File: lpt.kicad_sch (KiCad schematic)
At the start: 25 parts, among them J6 DB25 FEMALE, K1 TE_OJS_5V_10A, Q3 BC857, U2 74HC245, U4 LM358EDR2G, U5 ACSL-6400, U7 ACSL-6400

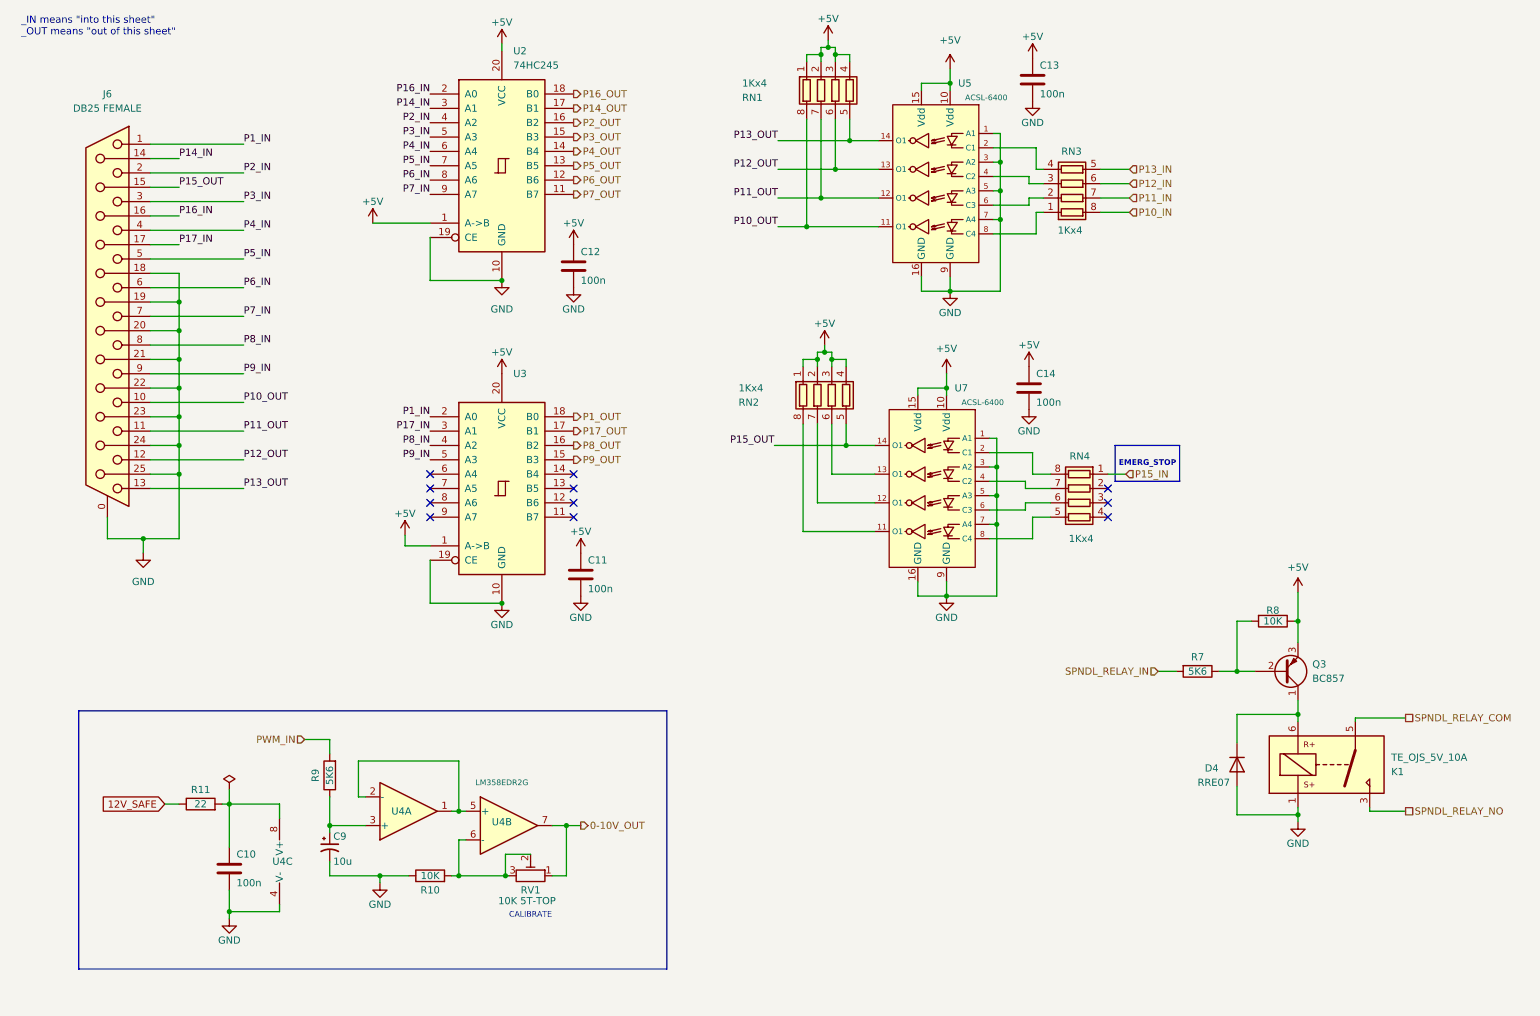
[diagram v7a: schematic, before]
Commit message: Scary file corruption turns out to be just bugs in eschema.
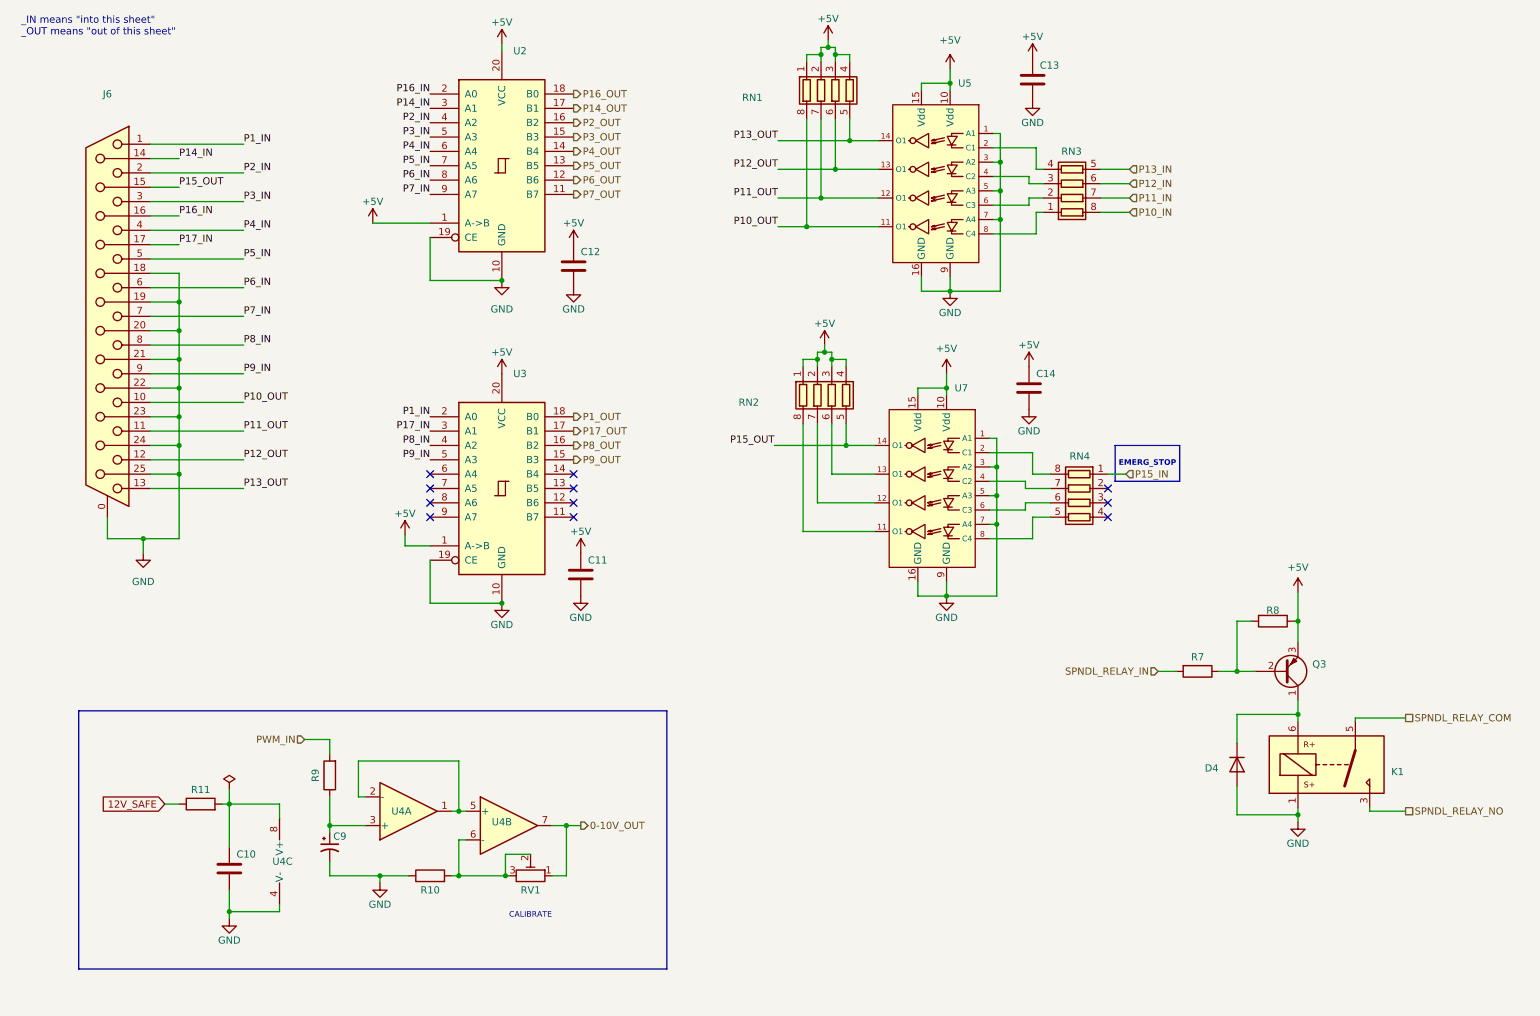
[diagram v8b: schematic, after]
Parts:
- C10, C11, C12, C13, C14: value 100n -> (none)
- C9: value 10u -> (none)
- D4: value RRE07 -> (none)
- J6: value DB25 FEMALE -> (none)
- K1: value TE_OJS_5V_10A -> (none)
- Q3: value BC857 -> (none)
- R10, R8: value 10K -> (none)
- R11: value 22 -> (none)
- R7, R9: value 5K6 -> (none)
- RN1, RN2, RN3, RN4: value 1Kx4 -> (none)
- RV1: value 10K 5T-TOP -> (none)
- U2: value 74HC245 -> (none)
- U4: value LM358EDR2G -> (none)
- U5, U7: value ACSL-6400 -> (none)
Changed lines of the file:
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@@
       (effects (font (size 1.27 1.27)) (justify left))
     )
-    (property "Value" "BC857" (id 1) (at 245.11 132.7149 0)
+    (property "Value" "" (id 1) (at 245.11 132.7149 0)
       (effects (font (size 1.27 1.27)) (justify left))
     )
@@
       (effects (font (size 1.27 1.27)) (justify left))
     )
-    (property "Value" "1Kx4" (id 1) (at 206.375 107.95 90)
+    (property "Value" "" (id 1) (at 206.375 107.95 90)
       (effects (font (size 1.27 1.27)) (justify left))
     )
@@
       (effects (font (size 1.27 1.27)) (justify left))
     )
-    (property "Value" "100n" (id 1) (at 115.57 62.23 0)
+    (property "Value" "" (id 1) (at 115.57 62.23 0)
       (effects (font (size 1.27 1.27)) (justify left))
     )
@@
       (effects (font (size 1.27 1.27)) (justify left))
     )
-    (property "Value" "100n" (id 1) (at 196.215 83.82 0)
+    (property "Value" "" (id 1) (at 196.215 83.82 0)
       (effects (font (size 1.27 1.27)) (justify left))
     )
@@
     (in_bom yes) (on_board yes)
     (property "Reference" "R10" (id 0) (at 88.9 170.18 90))
-    (property "Value" "10K" (id 1) (at 88.9 167.64 90))
+    (property "Value" "" (id 1) (at 88.9 167.64 90))
     (property "Footprint" "" (id 2) (at 88.9 169.418 90)
       (effects (font (size 1.27 1.27)) hide)
@@
     (in_bom yes) (on_board yes)
     (property "Reference" "RV1" (id 0) (at 106.68 170.18 90))
-    (property "Value" "10K 5T-TOP" (id 1) (at 106.045 172.085 90))
+    (property "Value" "" (id 1) (at 106.045 172.085 90))
     (property "Footprint" "" (id 2) (at 106.68 167.64 0)
       (effects (font (size 1.27 1.27)) hide)
@@
       (effects (font (size 1.27 1.27)) (justify left))
     )
-    (property "Value" "100n" (id 1) (at 54.61 168.91 0)
+    (property "Value" "" (id 1) (at 54.61 168.91 0)
       (effects (font (size 1.27 1.27)) (justify left))
     )
@@
     (in_bom yes) (on_board yes)
     (property "Reference" "U4" (id 0) (at 101.6 158.115 0))
-    (property "Value" "LM358EDR2G" (id 1) (at 101.6 151.13 0)
+    (property "Value" "" (id 1) (at 101.6 151.13 0)
       (effects (font (size 1 1)))
     )
@@
       (effects (font (size 1.27 1.27)) (justify left))
     )
-    (property "Value" "1Kx4" (id 1) (at 143.51 81.28 0)
+    (property "Value" "" (id 1) (at 143.51 81.28 0)
       (effects (font (size 1.27 1.27)) (justify left))
     )
@@
       (effects (font (size 1.27 1.27)) (justify left))
     )
-    (property "Value" "1Kx4" (id 1) (at 200.025 53.34 90)
+    (property "Value" "" (id 1) (at 200.025 53.34 90)
       (effects (font (size 1.27 1.27)) (justify left))
     )
@@
       (effects (font (size 1.27 1.27)) (justify left))
     )
-    (property "Value" "100n" (id 1) (at 196.85 29.21 0)
+    (property "Value" "" (id 1) (at 196.85 29.21 0)
       (effects (font (size 1.27 1.27)) (justify left))
     )
@@
     (in_bom yes) (on_board yes)
     (property "Reference" "R11" (id 0) (at 48.26 152.4 90))
-    (property "Value" "22" (id 1) (at 48.26 154.94 90))
+    (property "Value" "" (id 1) (at 48.26 154.94 90))
     (property "Footprint" "" (id 2) (at 48.26 156.718 90)
       (effects (font (size 1.27 1.27)) hide)
@@
       (effects (font (size 1.27 1.27)) (justify left))
     )
-    (property "Value" "ACSL-6400" (id 1) (at 190.5 83.82 0)
+    (property "Value" "" (id 1) (at 190.5 83.82 0)
       (effects (font (size 1 1)) (justify left))
     )
@@
     (in_bom yes) (on_board yes)
     (property "Reference" "R9" (id 0) (at 68.58 149.86 90))
-    (property "Value" "5K6" (id 1) (at 71.12 149.86 90))
+    (property "Value" "" (id 1) (at 71.12 149.86 90))
     (property "Footprint" "" (id 2) (at 72.898 149.86 90)
       (effects (font (size 1.27 1.27)) hide)
@@
       (effects (font (size 1.27 1.27)) (justify left))
     )
-    (property "Value" "1Kx4" (id 1) (at 144.145 27.305 0)
+    (property "Value" "" (id 1) (at 144.145 27.305 0)
       (effects (font (size 1.27 1.27)) (justify left))
     )
@@
       (effects (font (size 1.27 1.27)) (justify left))
     )
-    (property "Value" "74HC245" (id 1) (at 103.6194 24.13 0)
+    (property "Value" "" (id 1) (at 103.6194 24.13 0)
       (effects (font (size 1.27 1.27)) (justify left))
     )
@@
     (in_bom yes) (on_board yes)
     (property "Reference" "R8" (id 0) (at 238.125 120.65 90))
-    (property "Value" "10K" (id 1) (at 238.125 122.555 90))
+    (property "Value" "" (id 1) (at 238.125 122.555 90))
     (property "Footprint" "" (id 2) (at 238.125 120.777 90)
       (effects (font (size 1.27 1.27)) hide)
@@
     (in_bom yes) (on_board yes)
     (property "Reference" "R7" (id 0) (at 224.79 128.905 90))
-    (property "Value" "5K6" (id 1) (at 224.79 131.445 90))
+    (property "Value" "" (id 1) (at 224.79 131.445 90))
     (property "Footprint" "" (id 2) (at 224.79 129.667 90)
       (effects (font (size 1.27 1.27)) hide)
@@
       (effects (font (size 1.27 1.27)) (justify left))
     )
-    (property "Value" "ACSL-6400" (id 1) (at 191.135 29.845 0)
+    (property "Value" "" (id 1) (at 191.135 29.845 0)
       (effects (font (size 1 1)) (justify left))
     )
@@
       (effects (font (size 1.27 1.27)) (justify left))
     )
-    (property "Value" "LM358EDR2G" (id 1) (at 63.5 166.3699 0)
+    (property "Value" "" (id 1) (at 63.5 166.3699 0)
       (effects (font (size 1.27 1.27)) (justify left) hide)
     )
@@
       (effects (font (size 1.27 1.27)) (justify left))
     )
-    (property "Value" "RRE07" (id 1) (at 224.79 151.13 90)
+    (property "Value" "" (id 1) (at 224.79 151.13 90)
       (effects (font (size 1.27 1.27)) (justify left))
     )
@@
       (effects (font (size 1.27 1.27)) (justify left))
     )
-    (property "Value" "10u" (id 1) (at 71.755 165.1 0)
+    (property "Value" "" (id 1) (at 71.755 165.1 0)
       (effects (font (size 1.27 1.27)) (justify left))
     )
@@
       (effects (font (size 1.27 1.27)) (justify left))
     )
-    (property "Value" "100n" (id 1) (at 116.84 116.84 0)
+    (property "Value" "" (id 1) (at 116.84 116.84 0)
       (effects (font (size 1.27 1.27)) (justify left))
     )
@@
       (effects (font (size 1.27 1.27)) (justify left))
     )
-    (property "Value" "TE_OJS_5V_10A" (id 1) (at 259.08 146.6851 0)
+    (property "Value" "" (id 1) (at 259.08 146.6851 0)
       (effects (font (size 1.27 1.27)) (justify left))
     )
@@
     (in_bom yes) (on_board yes)
     (property "Reference" "U4" (id 0) (at 83.82 156.21 0))
-    (property "Value" "LM358EDR2G" (id 1) (at 87.63 151.13 0)
+    (property "Value" "" (id 1) (at 87.63 151.13 0)
       (effects (font (size 1 1)) hide)
     )
@@
     (in_bom yes) (on_board yes) (fields_autoplaced)
     (property "Reference" "J6" (id 0) (at 31.75 29.21 0))
-    (property "Value" "DB25 FEMALE" (id 1) (at 31.75 31.75 0))
+    (property "Value" "" (id 1) (at 31.75 31.75 0))
     (property "Footprint" "" (id 2) (at 31.75 68.58 0)
       (effects (font (size 1.27 1.27)) hide)
